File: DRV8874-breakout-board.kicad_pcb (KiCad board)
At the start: 2 copper layers, 27 x 40 mm, 16 parts, among them J101 M0_CONN, J102 Conn_01x02_Pin, J103 M0_CONN, J104 Conn_01x06_Pin, J105 PMODE

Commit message: Additional changes
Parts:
- C101: value 0.022uf -> 22nf
- moved R102 4.50 mm to (122.5, 102.0)
- moved R101 3.80 mm to (122.5, 98.7)
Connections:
- J104 pad 1: +3V3 -> nSLEEP
- J104 pad 2: GND -> nFAULT
- J104 pad 3: nSLEEP -> IPROPI
- J104 pad 4: nFAULT -> +3V3
- J104 pad 5: IPROPI -> GND
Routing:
- net nFAULT: track 13.0 -> 8.64 mm
- net IPROPI: track 14.4 -> 11.0 mm
- net +3V3: track 36.4 -> 33.3 mm, vias 3 -> 2
- net nSLEEP: track 10.8 -> 8.11 mm
- net GND: track 3.71 -> 6.34 mm, vias 19 -> 23
- net PMODE: track 16.9 -> 15.6 mm

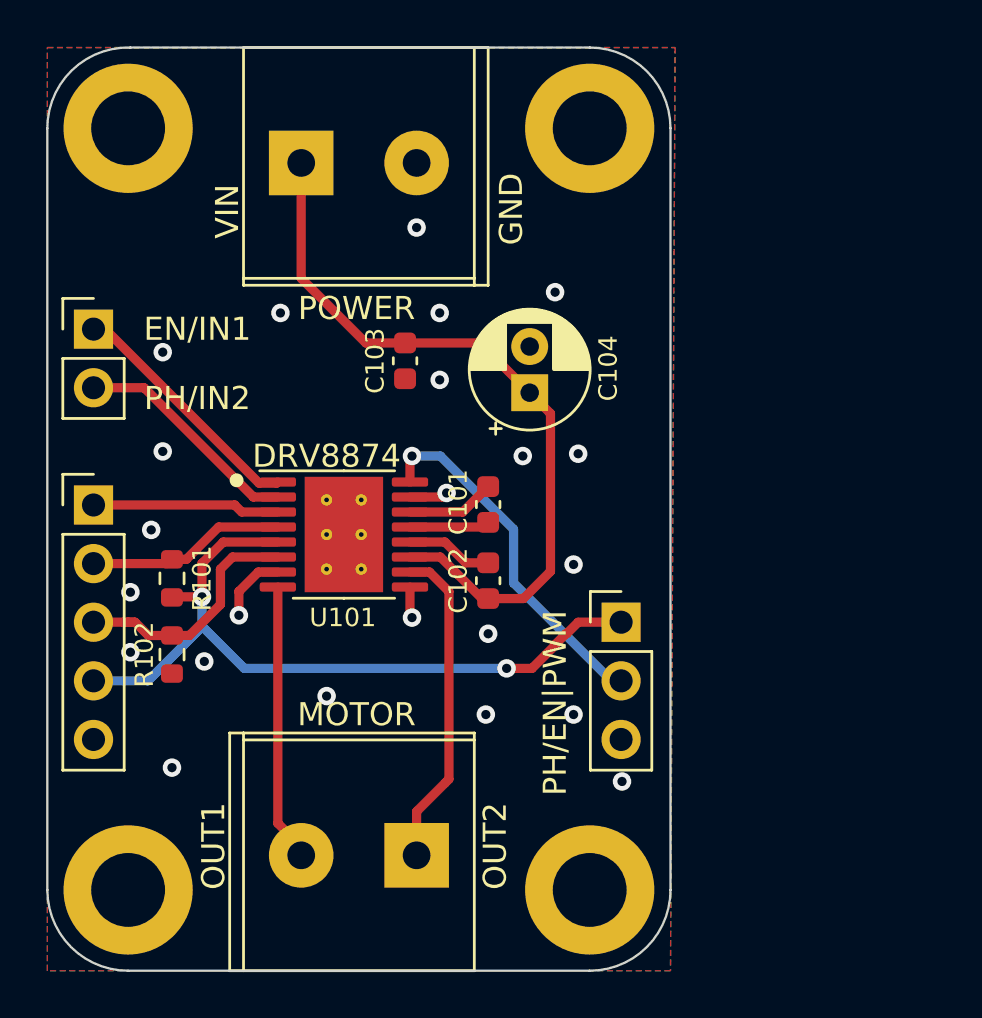
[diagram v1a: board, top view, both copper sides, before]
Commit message: First release version
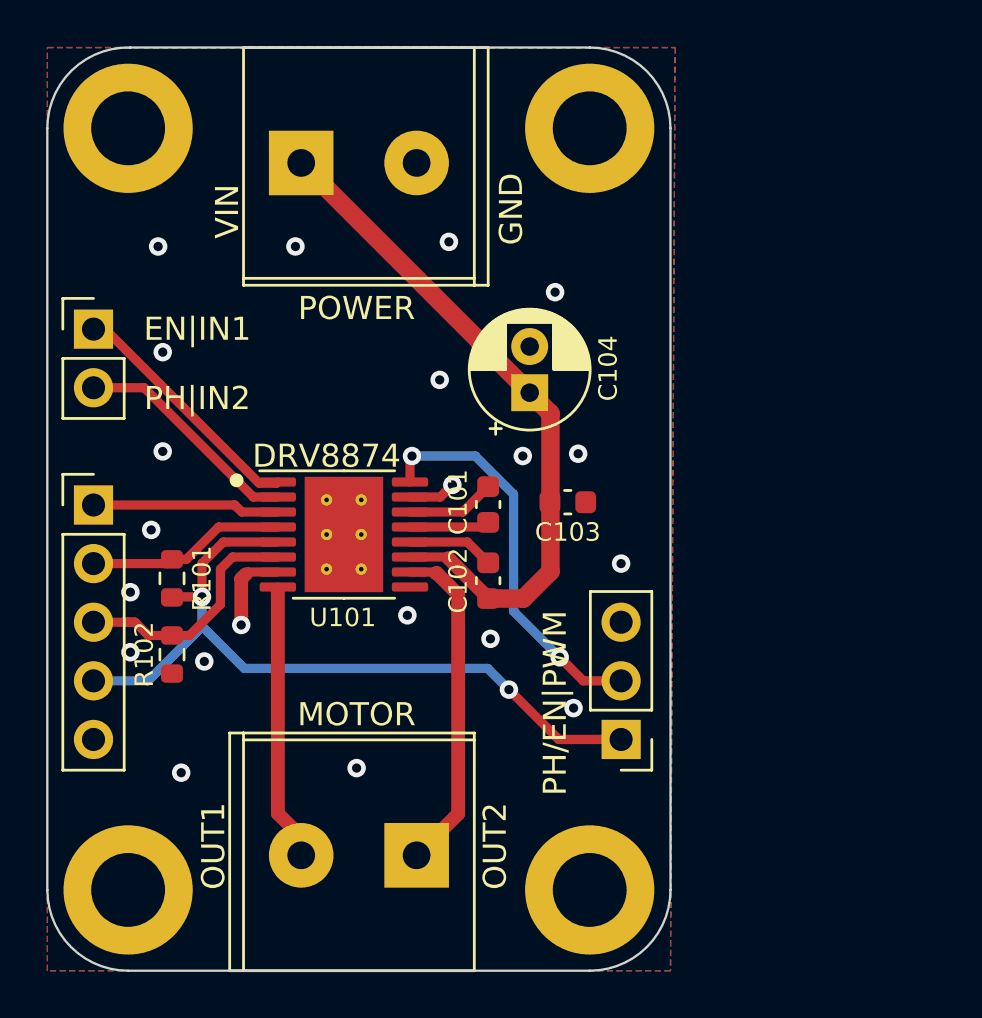
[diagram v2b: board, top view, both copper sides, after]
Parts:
- moved C103 9.34 mm to (139.7, 95.4), turned to 180 degrees
- moved J105 5.08 mm to (142.0, 105.7), turned to 180 degrees
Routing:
- net VMOTORS: track 32.4 -> 29.4 mm
- net Net-(J101-Pin_1): track 14.0 -> 15.9 mm
- net PMODE: track 15.6 -> 17.2 mm, vias 1 -> 2
- net GND: track 6.34 -> 5.77 mm, vias 23 -> 21

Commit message: Added external resistor
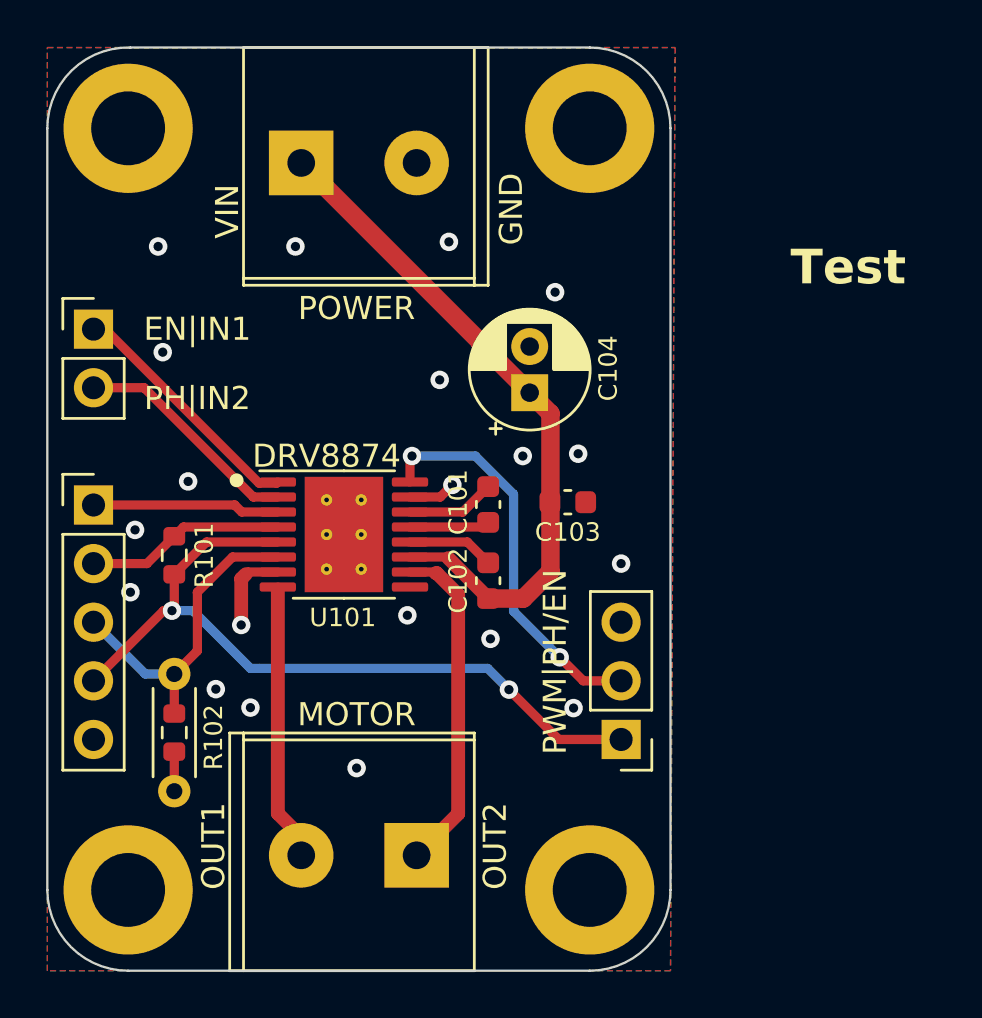
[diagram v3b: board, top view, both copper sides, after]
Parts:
- added R103: ~, Resistor_THT:R_Axial_DIN0204_L3.6mm_D1.6mm_P5.08mm_Horizontal, F.Cu at (122.6, 102.8)
- moved R102 3.38 mm to (122.6, 105.4)
- moved R101 1.00 mm to (122.6, 97.7)
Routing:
- net IPROPI: track 11.0 -> 14.2 mm
- net GND: track 5.77 -> 7.49 mm, vias 21 -> 20
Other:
- board text added: "Test"

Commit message: Fixed issue with text
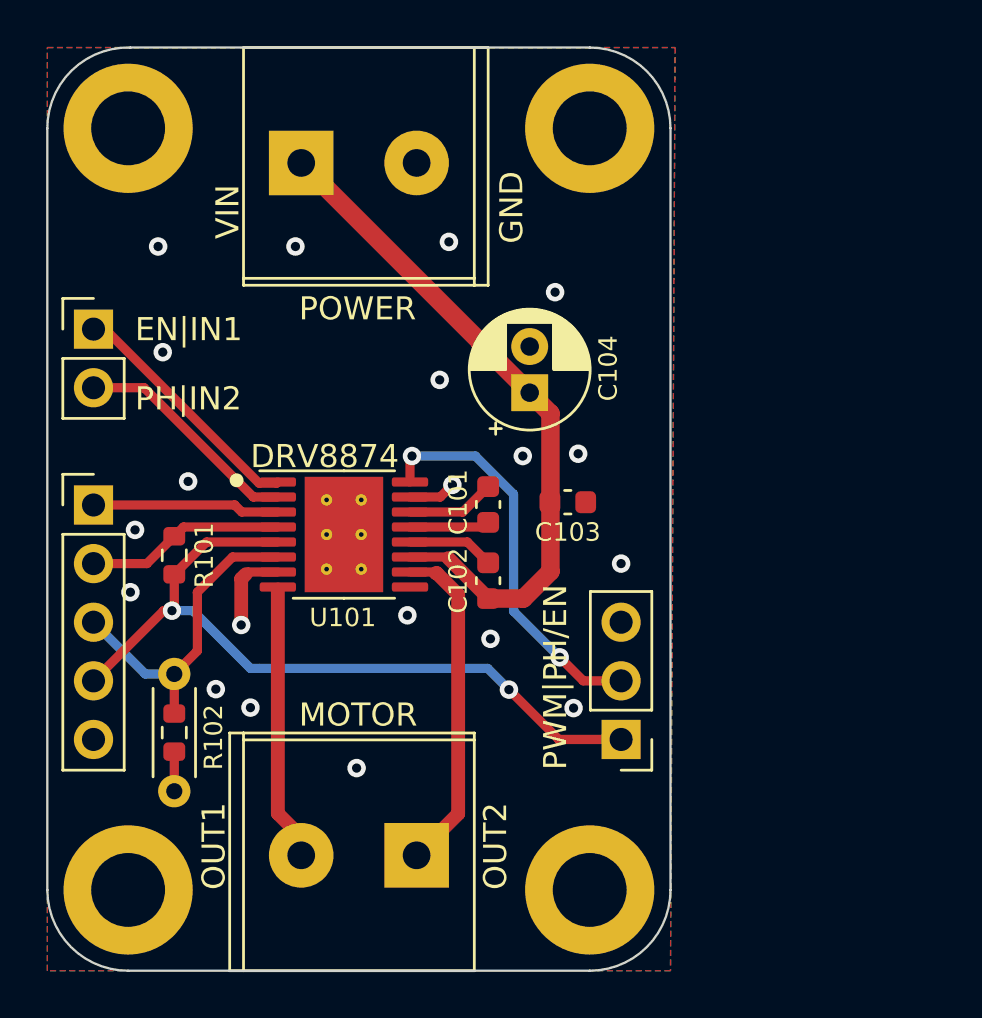
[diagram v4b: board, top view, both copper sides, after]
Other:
- board text added: "+"
- board text added: "+3.3V"
- board text added: "-"
- board text added: "1"
- board text added: "2"
- board text added: "DRV8874"
- board text added: "DRV8874 V1.0"
- board text added: "EN|IN1"
- board text added: "GND"
- board text added: "IPROPI"
- board text added: "MOTOR"
- board text added: "OUT1"
- board text added: "OUT2"
- board text added: "PH|IN2"
- board text added: "PMODE"
- board text added: "POWER"
- board text added: "PWM|PH/EN"
- board text added: "VIN"
- board text added: "VsReality Robotics"
- board text added: "nFAULT"
- board text added: "nSLEEP"
- board text removed: "Test"
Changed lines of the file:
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@@
     (pad_to_mask_clearance 0)
     (aux_axis_origin 117.1 115.7)
-    (grid_origin 117.3 86.1)
+    (grid_origin 117.1 75.7)
     (pcbplotparams
       (layerselection 0x00010fc_ffffffff)
@@
         (effects (font (size 1 1) (thickness 0.15)))
     )
-    (fp_text user "PMODE" (at 18.6 15.4) (layer "B.SilkS")
-        (effects (font (size 1 1) (thickness 0.15)) (justify mirror))
-    )
-    (fp_text user "VsReality Robotics" (at 11.6 7.82 90) (layer "B.SilkS")
-        (effects (font (size 1.5 1.5) (thickness 0.18)) (justify mirror))
-    )
-    (fp_text user "1" (at 8.8 25.8) (layer "B.SilkS")
-        (effects (font (size 1 1) (thickness 0.15)) (justify mirror))
-    )
-    (fp_text user "GND" (at 19.6 12.82) (layer "B.SilkS")
-        (effects (font (size 1 1) (thickness 0.15)) (justify mirror))
-    )
-    (fp_text user "+" (at 9 -9.7) (layer "B.SilkS")
-        (effects (font (size 1 1) (thickness 0.15)) (justify mirror))
-    )
-    (fp_text user "+" (at 17.4 4.3) (layer "B.SilkS")
-        (effects (font (size 1 1) (thickness 0.15)) (justify mirror))
-    )
-    (fp_text user "DRV8874 V1.0" (at 23 2.22 90) (layer "B.SilkS")
-        (effects (font (size 1 1) (thickness 0.15)) (justify mirror))
-    )
-    (fp_text user "nFAULT" (at 4.4 10.3) (layer "B.SilkS")
-        (effects (font (size 1 1) (thickness 0.15)) (justify mirror))
-    )
-    (fp_text user "nSLEEP" (at 4.5 7.8) (layer "B.SilkS")
-        (effects (font (size 1 1) (thickness 0.15)) (justify mirror))
-    )
-    (fp_text user "-" (at 14.1 -9.7) (layer "B.SilkS")
-        (effects (font (size 1 1) (thickness 0.15)) (justify mirror))
-    )
-    (fp_text user "GND" (at 3.4 18) (layer "B.SilkS")
-        (effects (font (size 1 1) (thickness 0.15)) (justify mirror))
-    )
-    (fp_text user "+3.3V" (at 4.2 15.4) (layer "B.SilkS")
-        (effects (font (size 1 1) (thickness 0.15)) (justify mirror))
-    )
-    (fp_text user "PH|IN2" (at 4.5 3) (layer "B.SilkS")
-        (effects (font (size 1 1) (thickness 0.15)) (justify mirror))
-    )
-    (fp_text user "2" (at 13.9 25.8) (layer "B.SilkS")
-        (effects (font (size 1 1) (thickness 0.15)) (justify mirror))
-    )
-    (fp_text user "+3.3V" (at 18.9 17.82) (layer "B.SilkS")
-        (effects (font (size 1 1) (thickness 0.15)) (justify mirror))
-    )
-    (fp_text user "EN|IN1" (at 4.5 0) (layer "B.SilkS")
-        (effects (font (size 1 1) (thickness 0.15)) (justify mirror))
-    )
-    (fp_text user "IPROPI" (at 4.3 12.8) (layer "B.SilkS")
-        (effects (font (size 1 1) (thickness 0.15)) (justify mirror))
-    )
-    (fp_text user "VIN" (at 5.8 -5.1 270) (layer "F.SilkS")
-        (effects (font (size 1 1) (thickness 0.15)))
-    )
-    (fp_text user "DRV8874" (at 10.1 5.5 180) (layer "F.SilkS")
-        (effects (font (size 1 1) (thickness 0.15)))
-    )
-    (fp_text user "GND" (at 18.1 -5.2 -90) (layer "F.SilkS")
-        (effects (font (size 1 1) (thickness 0.15)))
-    )
-    (fp_text user "PH|IN2" (at 4.5 3) (layer "F.SilkS")
-        (effects (font (size 1 1) (thickness 0.15)))
-    )
-    (fp_text user "PWM|PH/EN" (at 20 14.42 90) (layer "F.SilkS")
-        (effects (font (size 1 1) (thickness 0.15)))
-    )
-    (fp_text user "POWER" (at 11.4 -0.9) (layer "F.SilkS")
-        (effects (font (size 1 1) (thickness 0.15)))
-    )
-    (fp_text user "OUT1" (at 5.2 22.4 90) (layer "F.SilkS")
-        (effects (font (size 1 1) (thickness 0.15)))
-    )
-    (fp_text user "EN|IN1" (at 4.5 0) (layer "F.SilkS")
-        (effects (font (size 1 1) (thickness 0.15)))
-    )
-    (fp_text user "OUT2" (at 17.4 22.4 90) (layer "F.SilkS")
-        (effects (font (size 1 1) (thickness 0.15)))
-    )
-    (fp_text user "MOTOR" (at 11.4 16.7 180) (layer "F.SilkS")
-        (effects (font (size 1 1) (thickness 0.15)))
-    )
     (fp_text user "${REFERENCE}" (at 0 1.27 90) (layer "F.Fab")
         (effects (font (size 1 1) (thickness 0.15)))
@@
   (gr_arc (start 140.6 75.7) (mid 143.074874 76.725126) (end 144.1 79.2)
     (stroke (width 0.1) (type default)) (layer "Edge.Cuts"))
-  (gr_text "Test" (at 149.3 86.1) (layer "F.SilkS")
-    (effects (font (size 1.5 1.5) (thickness 0.3) bold) (justify left bottom))
+  (gr_text "1" (at 128.4 114.3) (layer "B.SilkS")
+    (effects (font (size 1 1) (thickness 0.15)) (justify left bottom mirror))
+  )
+  (gr_text "+3.3V" (at 125.5 103.9) (layer "B.SilkS")
+    (effects (font (size 1 1) (thickness 0.15)) (justify left bottom mirror))
+  )
+  (gr_text "PH|IN2" (at 126.4 91.5) (layer "B.SilkS")
+    (effects (font (size 1 1) (thickness 0.15)) (justify left bottom mirror))
+  )
+  (gr_text "nFAULT" (at 126.2 98.8) (layer "B.SilkS")
+    (effects (font (size 1 1) (thickness 0.15)) (justify left bottom mirror))
+  )
+  (gr_text "-" (at 132.6 78.8) (layer "B.SilkS")
+    (effects (font (size 1 1) (thickness 0.15)) (justify left bottom))
+  )
+  (gr_text "IPROPI" (at 125.9 101.3) (layer "B.SilkS")
+    (effects (font (size 1 1) (thickness 0.15)) (justify left bottom mirror))
+  )
+  (gr_text "+" (at 127.5 78.8) (layer "B.SilkS")
+    (effects (font (size 1 1) (thickness 0.15)) (justify left bottom))
+  )
+  (gr_text "DRV8874 V1.0" (at 142.7 84.9 90) (layer "B.SilkS")
+    (effects (font (size 1 1) (thickness 0.15)) (justify left bottom mirror))
+  )
+  (gr_text "+" (at 135.9 92.8) (layer "B.SilkS")
+    (effects (font (size 1 1) (thickness 0.15)) (justify left bottom))
+  )
+  (gr_text "2" (at 133.5 114.3) (layer "B.SilkS")
+    (effects (font (size 1 1) (thickness 0.15)) (justify left bottom mirror))
+  )
+  (gr_text "GND" (at 140.1 101.3) (layer "B.SilkS")
+    (effects (font (size 1 1) (thickness 0.15)) (justify left bottom mirror))
+  )
+  (gr_text "EN|IN1" (at 126.3 88.5) (layer "B.SilkS")
+    (effects (font (size 1 1) (thickness 0.15)) (justify left bottom mirror))
+  )
+  (gr_text "PMODE" (at 140.2 103.9) (layer "B.SilkS")
+    (effects (font (size 1 1) (thickness 0.15)) (justify left bottom mirror))
+  )
+  (gr_text "GND" (at 124 106.5) (layer "B.SilkS")
+    (effects (font (size 1 1) (thickness 0.15)) (justify left bottom mirror))
+  )
+  (gr_text "nSLEEP" (at 126.3 96.3) (layer "B.SilkS")
+    (effects (font (size 1 1) (thickness 0.15)) (justify left bottom mirror))
+  )
+  (gr_text "+3.3V" (at 140.2 106.3) (layer "B.SilkS")
+    (effects (font (size 1 1) (thickness 0.15)) (justify left bottom mirror))
+  )
+  (gr_text "VsReality Robotics" (at 131.6 85.4 90) (layer "B.SilkS")
+    (effects (font (size 1.5 1.5) (thickness 0.18)) (justify left bottom mirror))
+  )
+  (gr_text "DRV8874" (at 125.9 94) (layer "F.SilkS")
+    (effects (font (size 1 1) (thickness 0.15)) (justify left bottom))
+  )
+  (gr_text "POWER" (at 128 87.6) (layer "F.SilkS")
+    (effects (font (size 1 1) (thickness 0.15)) (justify left bottom))
+  )
+  (gr_text "MOTOR" (at 128 105.2) (layer "F.SilkS")
+    (effects (font (size 1 1) (thickness 0.15)) (justify left bottom))
+  )
+  (gr_text "PWM|PH/EN" (at 139.7 107 90) (layer "F.SilkS")
+    (effects (font (size 1 1) (thickness 0.15)) (justify left bottom))
+  )
+  (gr_text "GND" (at 137.8 84.2 90) (layer "F.SilkS")
+    (effects (font (size 1 1) (thickness 0.15)) (justify left bottom))
+  )
+  (gr_text "OUT2" (at 137.1 112.2 90) (layer "F.SilkS")
+    (effects (font (size 1 1) (thickness 0.15)) (justify left bottom))
+  )
+  (gr_text "EN|IN1" (at 120.9 88.5) (layer "F.SilkS")
+    (effects (font (size 1 1) (thickness 0.15)) (justify left bottom))
+  )
+  (gr_text "VIN" (at 125.5 84 90) (layer "F.SilkS")
+    (effects (font (size 1 1) (thickness 0.15)) (justify left bottom))
+  )
+  (gr_text "PH|IN2" (at 120.9 91.5) (layer "F.SilkS")
+    (effects (font (size 1 1) (thickness 0.15)) (justify left bottom))
+  )
+  (gr_text "OUT1" (at 124.9 112.2 90) (layer "F.SilkS")
+    (effects (font (size 1 1) (thickness 0.15)) (justify left bottom))
   )
   (segment (start 132.8125 96.475) (end 136 96.475) (width 0.4) (layer "F.Cu") (net 1))

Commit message: Added trace zones
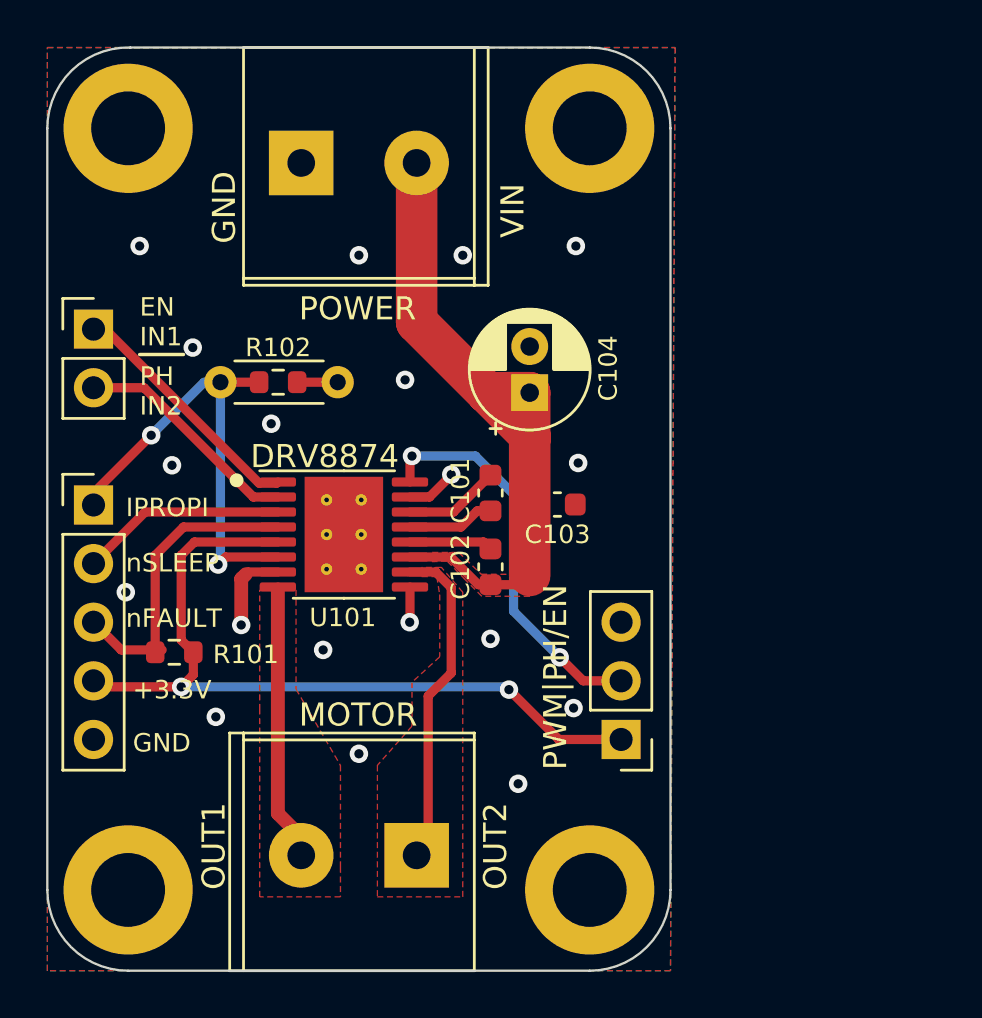
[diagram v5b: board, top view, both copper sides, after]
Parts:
- moved R102 15.8 mm to (127.1, 90.2), turned to 0 degrees
- moved R103 12.8 mm to (124.6, 90.2), turned to 0 degrees
- moved R101 4.20 mm to (122.6, 101.9), turned to 180 degrees
- moved C102 0.61 mm to (136.3, 98.2)
- moved C101 0.51 mm to (136.3, 95.0)
- moved C103 0.46 mm to (139.2, 95.5)
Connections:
- net Net-(J101-Pin_1) renamed OUT2
- net Net-(J101-Pin_2) renamed OUT1
- J103 pad 1: VMOTORS -> GND
- J103 pad 2: GND -> VMOTORS
- J104 pad 1: nSLEEP -> IPROPI
- J104 pad 2: nFAULT -> nSLEEP
- J104 pad 3: IPROPI -> nFAULT
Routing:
- net IPROPI: track 14.2 -> 21.0 mm, vias 0 -> 2
- net nFAULT: track 8.64 -> 13.5 mm
- net GND: track 7.49 -> 9.21 mm, vias 20 -> 19
- net OUT2: track 15.9 -> 14.3 mm
- net +3V3: track 33.5 -> 34.7 mm
- net nSLEEP: track 8.11 -> 8.91 mm
- added copper zone on F.Cu, net OUT1
- added copper zone on F.Cu, net OUT2
- added copper zone on F.Cu, net VMOTORS
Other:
- board text added: "EN IN1"
- board text added: "PH IN2"
- board text removed: "EN|IN1"
- board text removed: "PH|IN2"
